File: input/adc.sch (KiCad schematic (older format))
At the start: 1 part

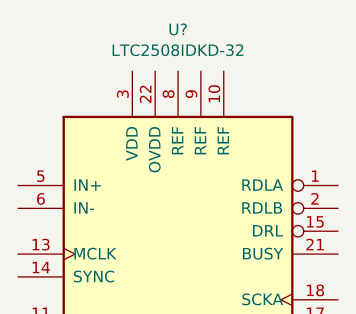
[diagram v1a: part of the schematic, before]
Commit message: Continuing work on input board, also added some design files and PDF documentation for the prototype source and sensor.  Deleted various spurious kicad project files.  The main project for the input board is now input_board.pro.
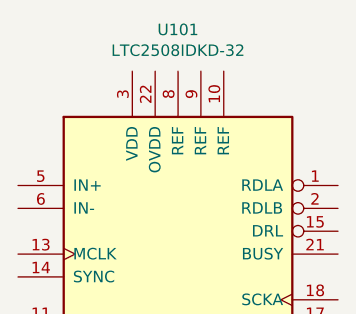
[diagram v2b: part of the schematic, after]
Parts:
- gave numbers to parts that had none: 1
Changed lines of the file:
@@
 EESchema Schematic File Version 4
-LIBS:input-cache
-LIBS:in_amp-cache
+LIBS:input_channel-cache
 EELAYER 29 0
 EELAYER END
@@
 P 8800 3450
 AR Path="/5DA7BB2A" Ref="U?"  Part="1"
-AR Path="/5DA78AA2/5DA7BB2A" Ref="U?"  Part="1"
-F 0 "U?" H 8800 4531 50  0000 C CNN
+AR Path="/5DA78AA2/5DA7BB2A" Ref="U101"  Part="1"
+F 0 "U101" H 8800 4531 50  0000 C CNN
 F 1 "LTC2508IDKD-32" H 8800 4440 50  0000 C CNN
 F 2 "Package_DFN_QFN:DFN-24-1EP_4x7mm_P0.5mm_EP2.64x6.44mm" H 7850 2500 50  0001 L CNN
@@
 P 8600 4600
 AR Path="/5DA7BB38" Ref="#PWR?"  Part="1"
-AR Path="/5DA78AA2/5DA7BB38" Ref="#PWR?"  Part="1"
-F 0 "#PWR?" H 8600 4350 50  0001 C CNN
+AR Path="/5DA78AA2/5DA7BB38" Ref="#PWR0101"  Part="1"
+F 0 "#PWR0101" H 8600 4350 50  0001 C CNN
 F 1 "GNDA" H 8605 4427 50  0000 C CNN
 F 2 "" H 8600 4600 50  0001 C CNN

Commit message: More work on input board
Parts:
- added C? (x2): 47uF, Capacitor_SMD:C_1210_3225Metric, symbol Device:C_Small
- added C? (x2): 10uF, Capacitor_SMD:C_0603_1608Metric, symbol Device:C_Small
- added C? (x3): 100nF, Capacitor_SMD:C_0603_1608Metric, symbol Device:C_Small
- added C? (x2): 6.8nF, Capacitor_SMD:C_1206_3216Metric, symbol Device:C_Small
- added C?: OPT, Capacitor_SMD:C_1206_3216Metric, symbol Device:C_Small
- added R? (x2): 10, symbol Device:R_US
- added R? (x2): 33, Capacitor_SMD:C_0402_1005Metric, symbol Device:R_US
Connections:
- net GNDA: now also U101.1 (RDLA), U101.2 (RDLB), C?.1, C?.2, C?.2, C?.2, C?.2, C?.2, C?.2, C?.2, C?.2
- net reference: now reaches U101.10 (REF)
- net reference: now also U101.8 (REF), U101.9 (REF), C?.1, C?.1, C?.1
- net SEL0: now reaches U101.11 (SEL0)
- net SEL1: now reaches U101.12 (SEL1)
- net MCLK: now reaches U101.13 (MCLK)
- net SYNC: now reaches U101.14 (SYNC)
- net DRL: now reaches U101.15 (DRL)
- net at U101.17 (SDOA): now also R?.2
- net SCKA: now reaches U101.18 (SCKA)
- net SCKB: now reaches U101.19 (SCKB)
- net at U101.20 (SDOB): now also R?.2
- net BUSY: now reaches U101.21 (BUSY)
- net OVDD: now reaches U101.22 (OVDD)
- net OVDD: now also C?.1, C?.1
- net VDD: now reaches U101.3 (VDD)
- net VDD: now also C?.1, C?.1
- net at U101.5 (IN+): now also C?.1, C?.1, R?.1
- net at U101.6 (IN-): now also C?.2, C?.2, R?.1
- new net +in: R?.2
- new net -in: R?.2
- new net SDOA: R?.1
- new net SDOB: R?.1
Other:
- note added: "LTC2508-32 is the high-decimation version, we are using LTC2512-24, which\nis only low decimation. The pinout and footprint is identical."
- moved on the sheet: U101

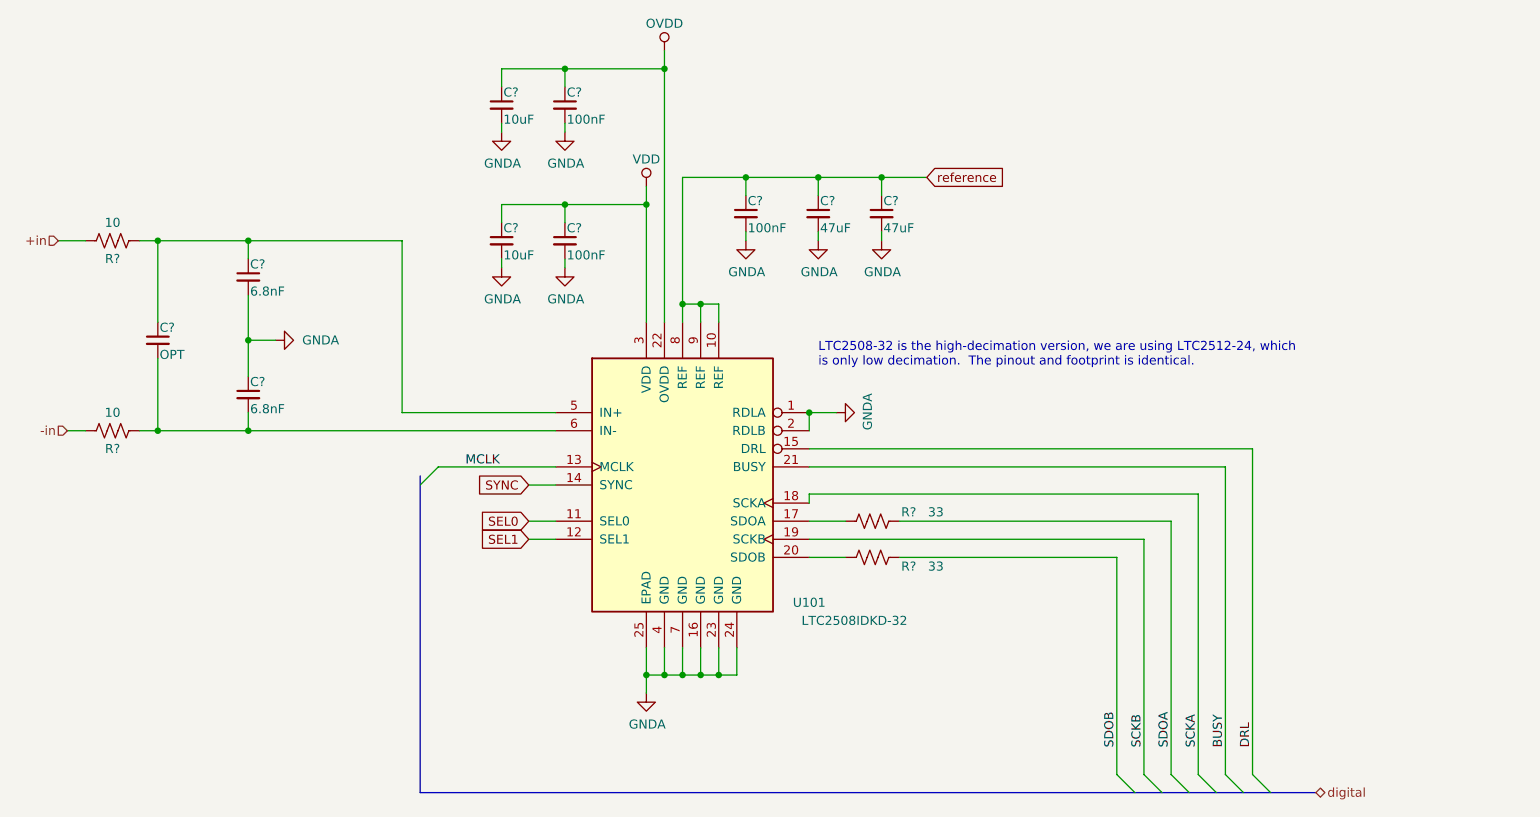
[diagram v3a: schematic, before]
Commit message: Mainly work on the top level of the input board, attaching signals to the channels, digital I/O.  Decided to use Eurocard 64 pin type B connector for the connection to the main board.  See input_board_pinout.txt.
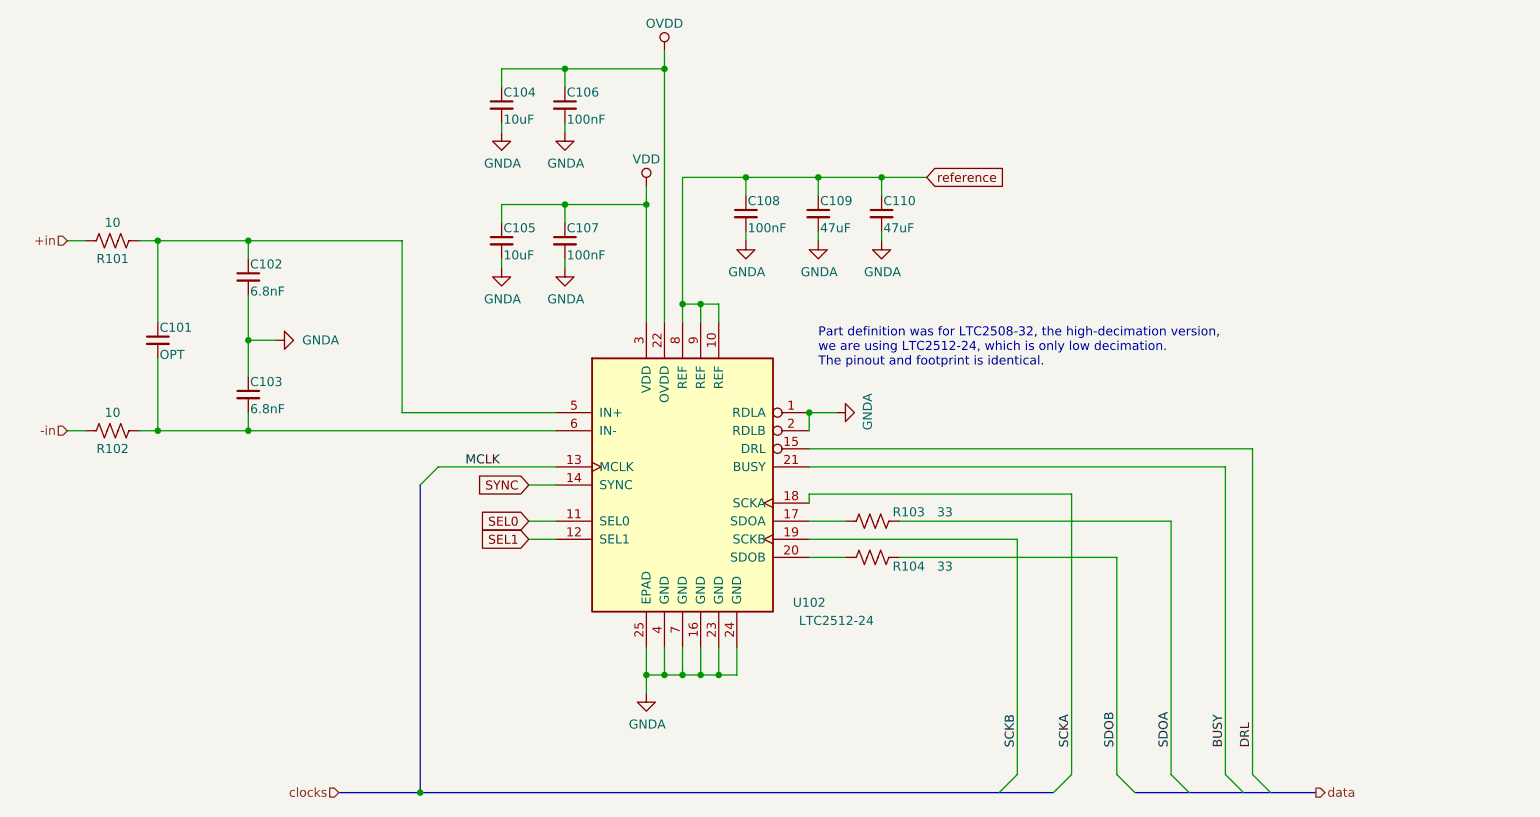
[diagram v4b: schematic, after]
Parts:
- removed C? (x2): 47uF, Capacitor_SMD:C_1210_3225Metric, symbol Device:C_Small
- removed C?: 10uF, Capacitor_SMD:C_0603_1608Metric, symbol Device:C_Small
- removed C?: 100nF, Capacitor_SMD:C_0603_1608Metric, symbol Device:C_Small
- removed C?: 6.8nF, Capacitor_SMD:C_1206_3216Metric, symbol Device:C_Small
- removed C?: OPT, Capacitor_SMD:C_1206_3216Metric, symbol Device:C_Small
- removed R? (x2): 10, symbol Device:R_US
- removed R? (x2): 33, Capacitor_SMD:C_0402_1005Metric, symbol Device:R_US
- added C101: OPT, Capacitor_SMD:C_1206_3216Metric, symbol Device:C_Small
- added C102: 6.8nF, Capacitor_SMD:C_1206_3216Metric, symbol Device:C_Small
- added C105: 10uF, Capacitor_SMD:C_0603_1608Metric, symbol Device:C_Small
- added C108: 100nF, Capacitor_SMD:C_0603_1608Metric, symbol Device:C_Small
- added C109, C110: 47uF, Capacitor_SMD:C_1210_3225Metric, symbol Device:C_Small
- added R101, R102: 10, symbol Device:R_US
- added R103, R104: 33, Capacitor_SMD:C_0402_1005Metric, symbol Device:R_US
- U101: value LTC2508IDKD-32 -> LTC2512-24
- gave numbers to parts that had none: 4
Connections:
- net +in: now also R101.2
- net -in: now also R102.2
- net GNDA: now also C102.2, C105.2, C108.2, C109.2, C110.2
- net SDOA: now also R103.1
- net SDOB: now also R104.1
- net VDD: now also C105.1
- net reference: now also C108.1, C109.1, C110.1
- net at U101.17 (SDOA): now also R103.2
- net at U101.20 (SDOB): now also R104.2
- net at U101.5 (IN+): now also C101.1, C102.1, R101.1
- net at C103.2, U101.6 (IN-): now also C101.2, R102.1
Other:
- note added: "Part definition was for LTC2508-32, the high-decimation version, \nwe are using LTC2512-24, which is only low decimation. \nThe pinout and footprint is identical."
- note removed: "LTC2508-32 is the high-decimation version, we are using LTC2512-24, which\nis only low decimation. The pinout and footprint is identical."

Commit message: Still beating into overall shape.  This is a checkpoint before modifying the analog signal chain to fold the diff amp and antialias into the driver, going to a full differential path.
Overall: Changes to component attributes to reduce duplicates in BOM, and added links to Digikey and datasheets.

board_connector.sch: Added reference input pins, decimation SEL lines.

in_filter.sch:
Fixed BIST feedback to be taken at the top of each injection resistor (4 lines, not 2)

input_board.sch:
Added some missing connections and no-connects.

power_budget.xlsx:
Much more elaborate now, models effect of input levels on load currents, computes currents and total power, for several variants.

reference_buffer.sch:
Updated with booster sink transistor to handle sourcing into reference by ADC clamp diodes.

simetrix/:
Added supply_negative.wxsch and supply_positive.wxsch, which are concepts for low noise lowish dropout regulators for the analog rails.  Other simetrix modifications are cosmetic.
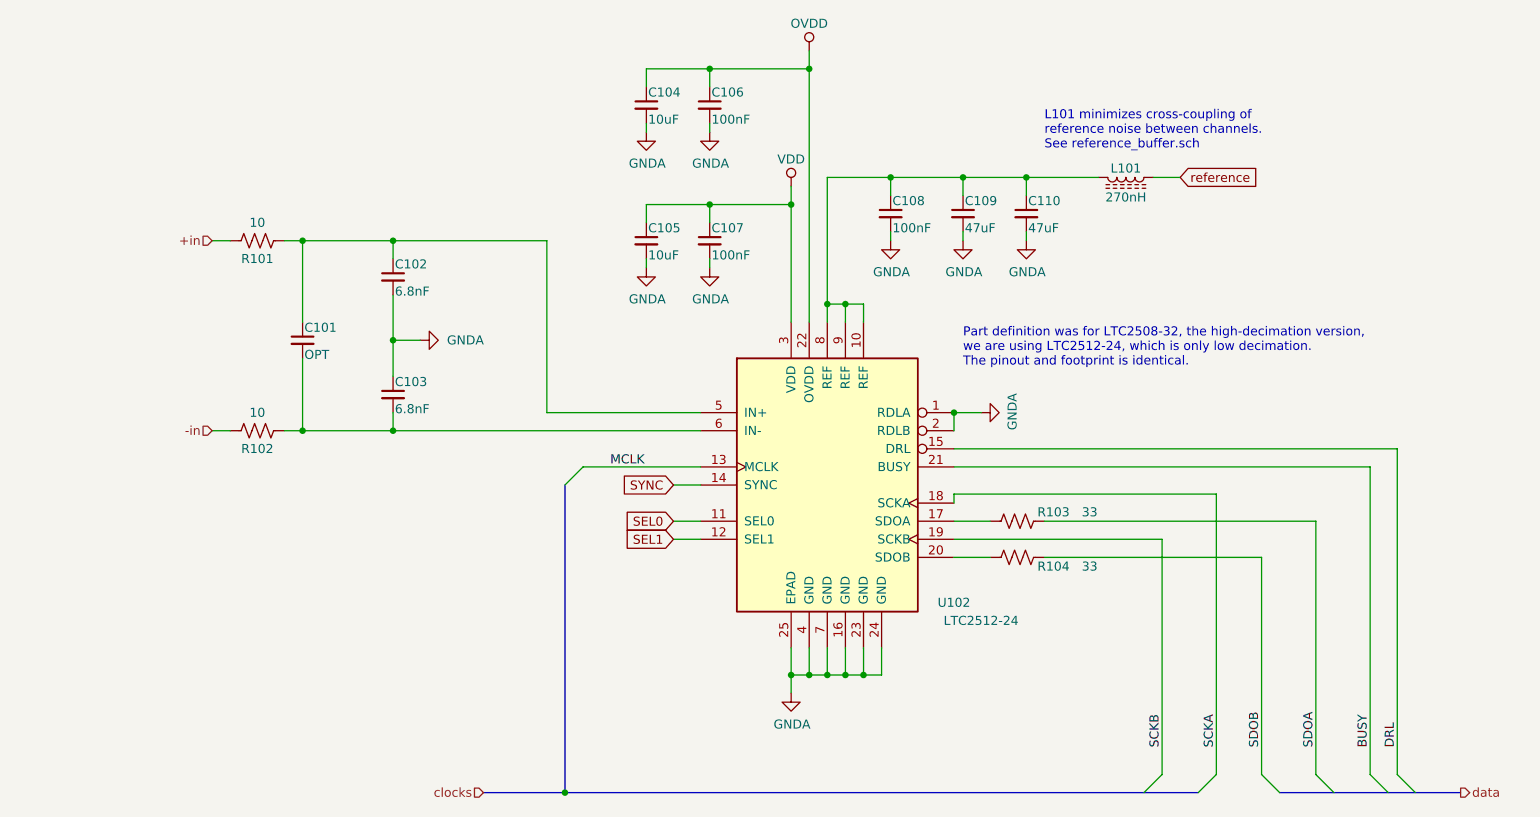
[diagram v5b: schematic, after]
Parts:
- added L101: 270nH, Inductor_SMD:L_0603_1608Metric, symbol Device:L_Core_Ferrite
- R101, R102: footprint (none) -> Resistor_SMD:R_0805_2012Metric; Digikey (none) -> 541-10TACT-ND; MPN (none) -> CRCW080510R0JNEAHP; Notes (none) -> Thick film surge resist
- R103, R104: footprint Capacitor_SMD:C_0402_1005Metric -> Resistor_SMD:R_0603_1608Metric
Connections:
- net reference: now also L101.1; no longer C108.1, C109.1, C110.1, U101.10 (REF), U101.8 (REF), U101.9 (REF)
- new net: C108.1, C109.1, C110.1, L101.2, U101.10 (REF), U101.8 (REF), U101.9 (REF)
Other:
- note added: "L101 minimizes cross-coupling of \nreference noise between channels.\nSee reference_buffer.sch"
- moved on the sheet: C101, C102, C103, C104, C105, C106, C107, C108, C109, C110, R101, R102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

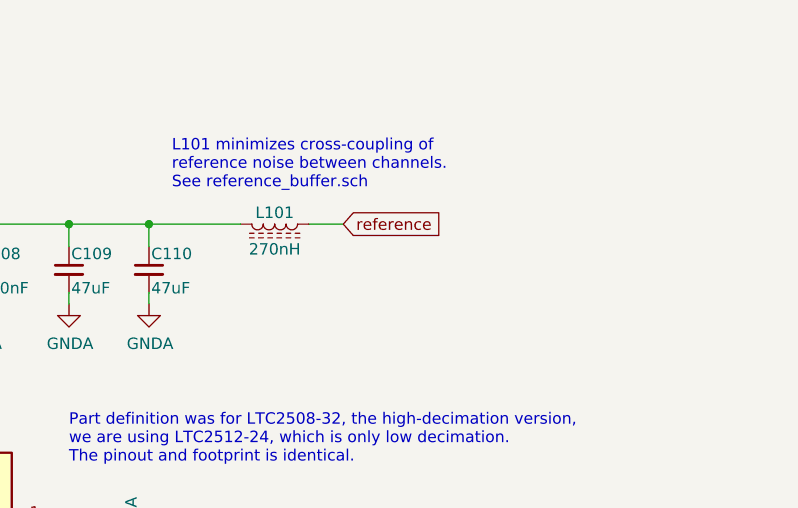
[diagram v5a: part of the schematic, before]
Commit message: Changes mostly related to avoiding excess power consumption.  This is mainly by limiting the signal swing to 0..5V and using asymmetric supplies of -4V and +8V.  (Perhaps we can reduce these to 3/7 V.)  Also, I got rid of two stages in the input signal path.
power_budget.xlsx
power.sch
reference_buffer.sch:
Changes related to the new supply voltages, and start on the power supply section.

input_channel.sch
in_amp.sch
antialias_driver.sch:
Reworked the input signal chain to keep a full differential path, rolling the antialias filter
into the ADC driver.  Also, related to change to lower asymmetrical supply voltages, there is
no 20V PP anywhere (the this was for benefit of the antialias filter noise, but that stage is gone).  Also, added zener clamp on VREF in driver.

in_filter.sch: added missing DC bias resistors.
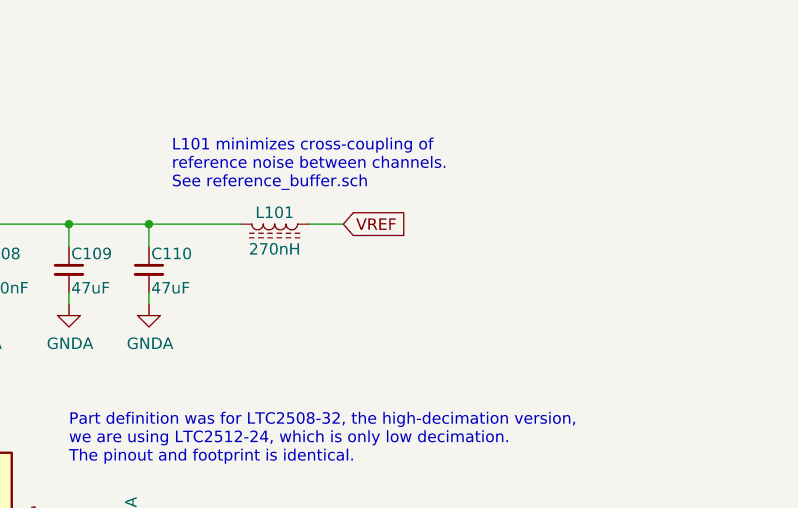
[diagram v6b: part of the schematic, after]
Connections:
- net reference renamed VREF
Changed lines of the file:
@@
 LIBS:input_board-cache
 LIBS:input_channel-cache
+LIBS:reference_buffer-cache
 EELAYER 29 0
 EELAYER END
 $Descr A4 11693 8268
 encoding utf-8
-Sheet 3 10
+Sheet 3 11
 Title ""
 Date ""
@@
 $EndComp
 Text GLabel 8850 2300 2    50   Input ~ 0
-reference
+VREF
 Wire Wire Line
 	6900 3000 7000 3000
